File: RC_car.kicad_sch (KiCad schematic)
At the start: 31 parts, among them J1 Conn_02x04_Row_Letter_First, J10 Conn_01x01, J11 MP1584_IN+, J12 MP1584_IN-, J13 MP1584_OUT-, J14 MP1584_OUT+, J2 Screw_Terminal_01x02, J3 Screw_Terminal_01x02, J4 Conn_01x03, J7 Conn_01x01, J8 Conn_01x01, J9 Conn_01x01, U2 L298N, U3 LM2596T-5

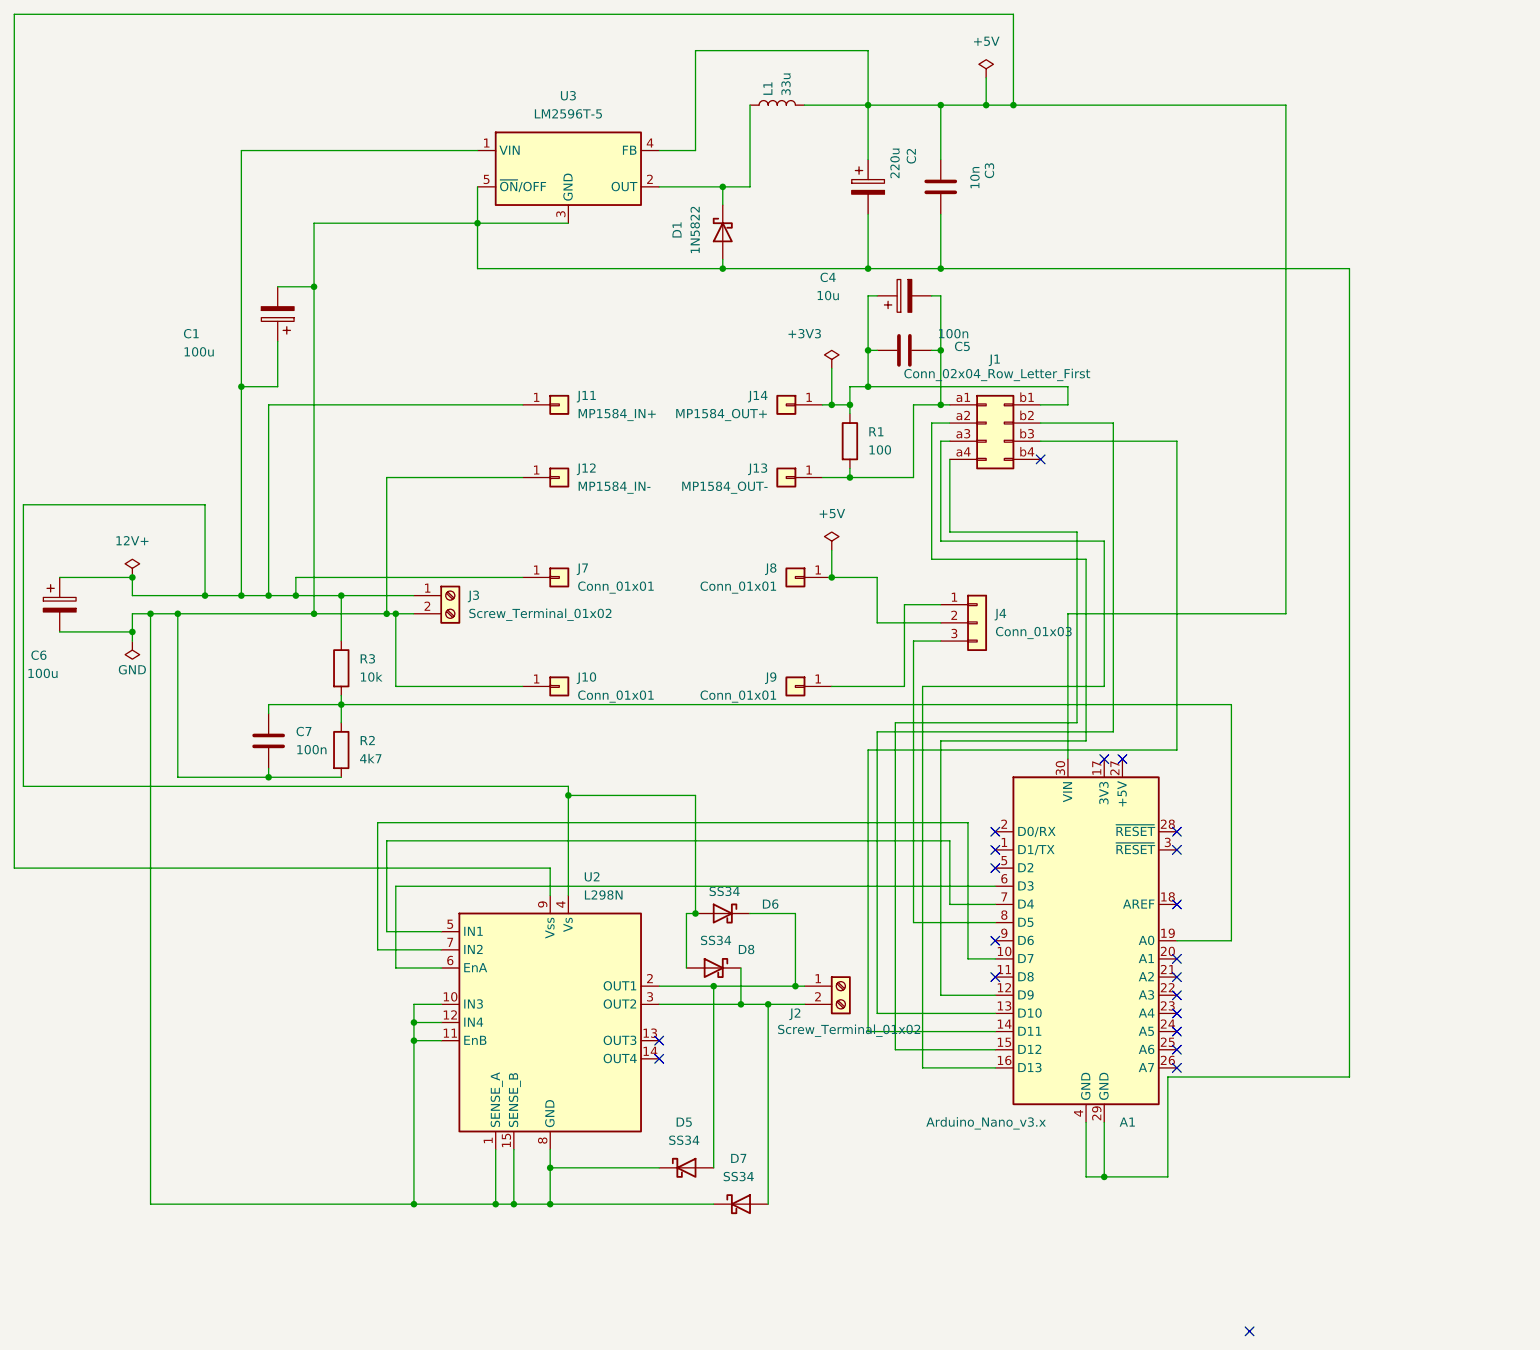
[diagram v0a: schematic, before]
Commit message: Fixed diodes orientation, rework grounding
- reversed all 4 SS34 flyback diodes on L298N outputs
- Nano now powered via 5V pin instead of VIN
- unified ground islands with power:GND symbols
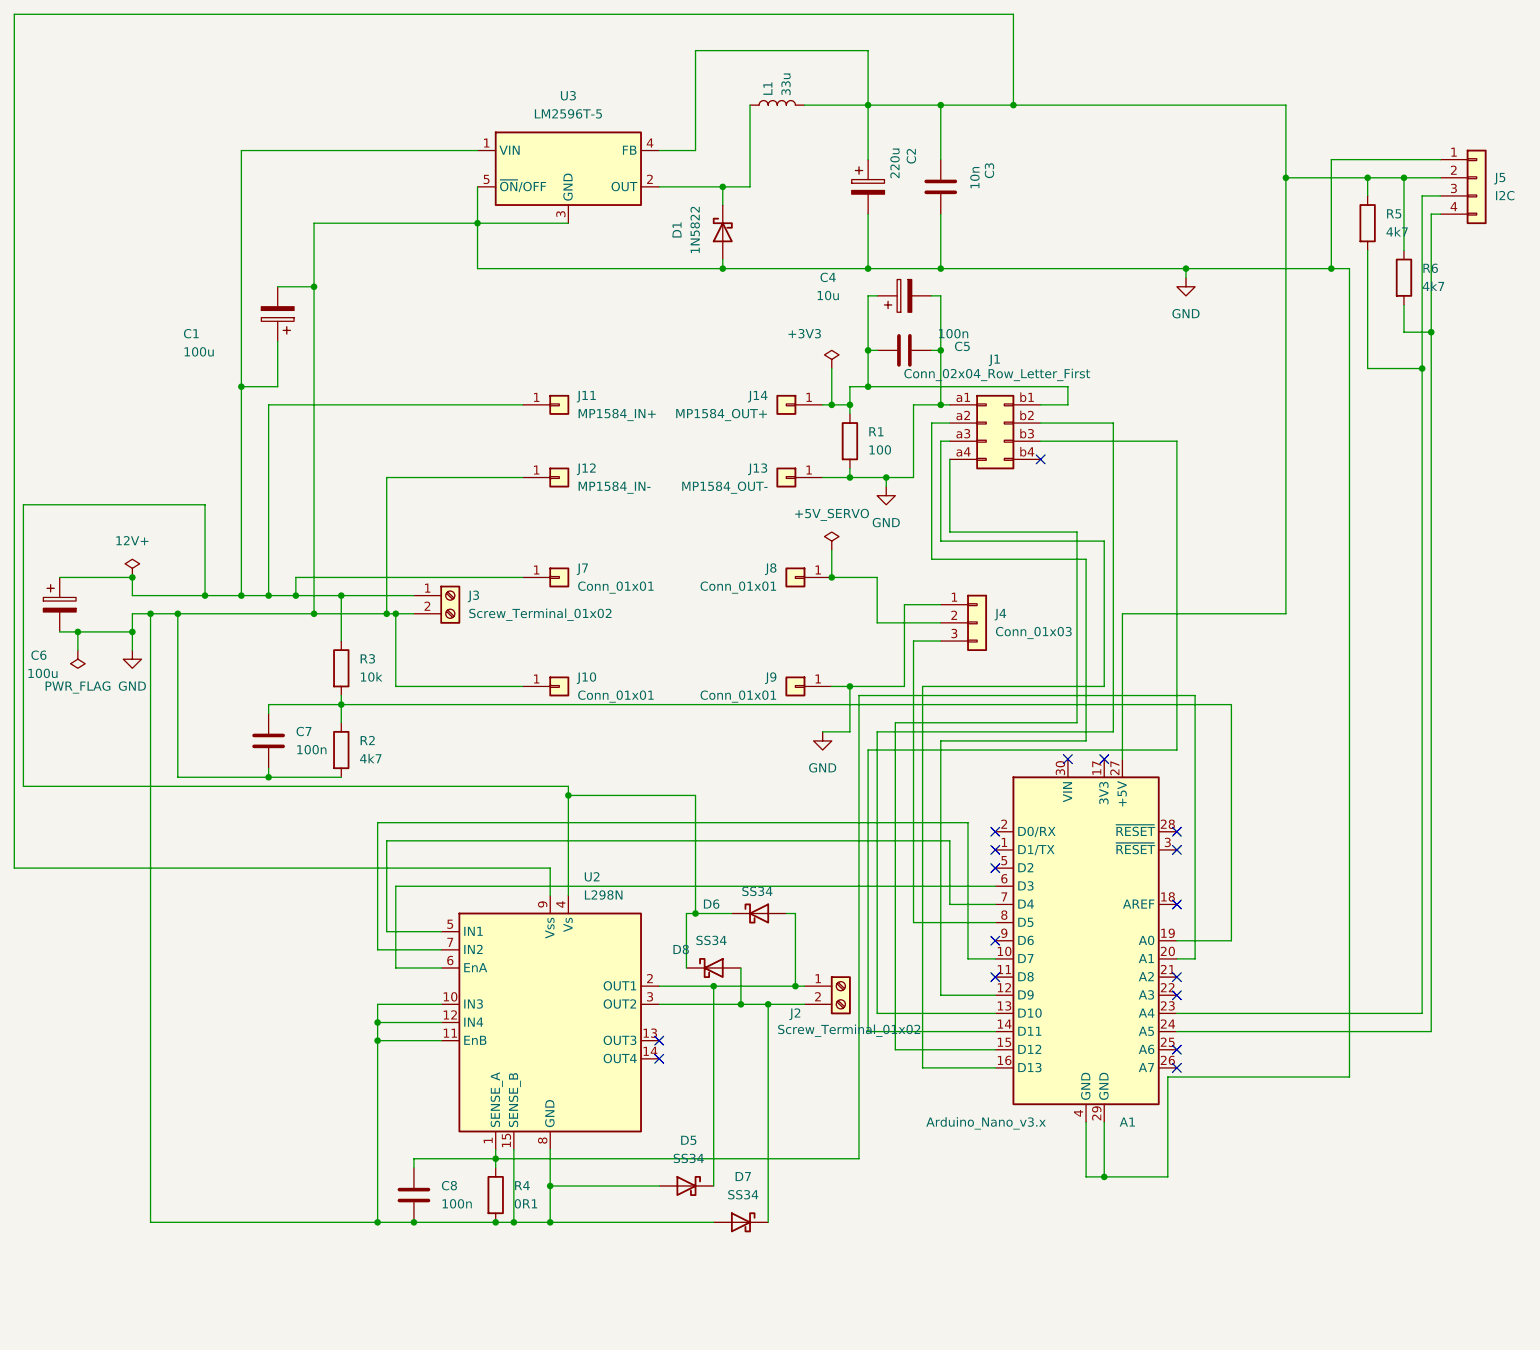
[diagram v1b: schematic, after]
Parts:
- added C8: 100n, symbol Device:C
- added J5: I2C, symbol Connector_Generic:Conn_01x04
- added R4: 0R1, symbol Device:R
- added R5, R6: 4k7, symbol Device:R
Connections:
- net at C1.1, C6.1, J11.1 (Pin_1)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: now also D6.1 (K), D8.1 (K); no longer D6.2 (A), D8.2 (A)
- net GND: now reaches A1.29 (GND), A1.4 (GND), C1.2, C2.2, C3.2, C6.2, C7.2, D1.2 (A), J10.1 (Pin_1), J12.1 (Pin_1), J3.2 (Pin_2), R2.2, U2.10 (IN3), U2.11 (EnB), U2.12 (IN4), U2.15 (SENSE_B), U2.8 (GND), U3.3 (GND), U3.5 (~{ON}/OFF)
- net GND: now also C4.2, C5.1, D5.2 (A), D7.2 (A), J1.a1 (Pin_a1), J13.1 (Pin_1), J4.1 (Pin_1), J9.1 (Pin_1), R1.2, C8.2, J5.1 (Pin_1), R4.2; no longer D5.1 (K), D7.1 (K), U2.1 (SENSE_A)
- net at J2.1 (Pin_1), U2.2 (OUT1): now also D5.1 (K), D6.2 (A); no longer D5.2 (A), D6.1 (K)
- net at C2.1, C3.1, L1.2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: now also A1.27 (+5V), J5.2 (Pin_2), R5.1, R6.1; no longer A1.30 (VIN)
- net at J2.2 (Pin_2), U2.3 (OUT2): now also D7.1 (K), D8.2 (A); no longer D7.2 (A), D8.1 (K)
- net at A1.20 (A1): now also U2.1 (SENSE_A), C8.1, R4.1
- net at A1.23 (A4): now also J5.3 (Pin_3), R5.2
- net at A1.24 (A5): now also J5.4 (Pin_4), R6.2
- no-connect marks 21 -> 17
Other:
- moved on the sheet: D5, D6, D7

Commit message: Improve schematic readability
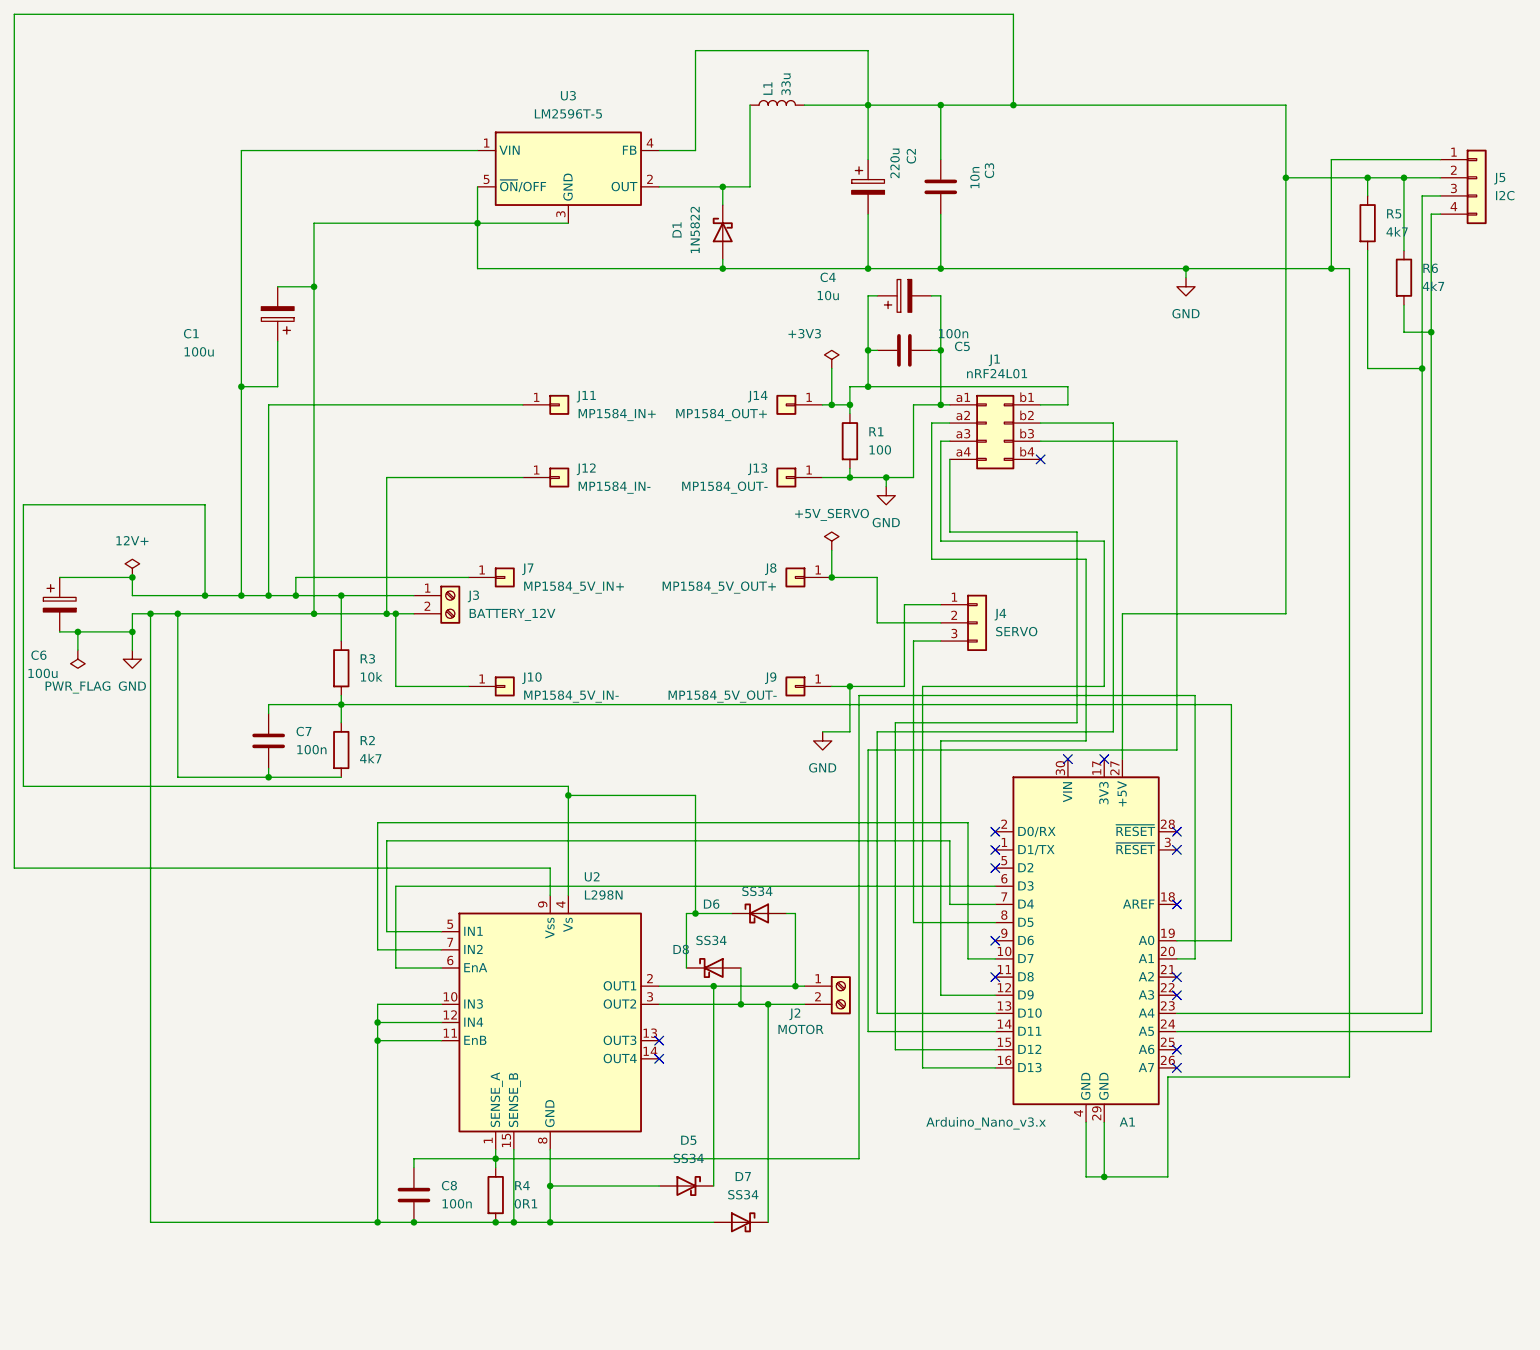
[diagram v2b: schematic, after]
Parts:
- J1: value Conn_02x04_Row_Letter_First -> nRF24L01
- J10: value Conn_01x01 -> MP1584_5V_IN-
- J2: value Screw_Terminal_01x02 -> MOTOR
- J3: value Screw_Terminal_01x02 -> BATTERY_12V
- J4: value Conn_01x03 -> SERVO
- J7: value Conn_01x01 -> MP1584_5V_IN+
- J8: value Conn_01x01 -> MP1584_5V_OUT+
- J9: value Conn_01x01 -> MP1584_5V_OUT-
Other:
- moved on the sheet: J10, J7
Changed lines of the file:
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@@
 	(wire
 		(pts
-			(xy 85.09 95.25) (xy 53.34 95.25)
+			(xy 77.47 95.25) (xy 53.34 95.25)
 		)
 		(stroke
@@
 	(wire
 		(pts
-			(xy 85.09 110.49) (xy 67.31 110.49)
+			(xy 77.47 110.49) (xy 67.31 110.49)
 		)
 		(stroke
@@
 			)
 		)
-		(property "Value" "Screw_Terminal_01x02"
+		(property "Value" "BATTERY_12V"
 			(at 77.47 100.3299 0)
 			(show_name no)
@@
 	(symbol
 		(lib_id "Connector_Generic:Conn_01x01")
-		(at 90.17 110.49 0)
+		(at 82.55 110.49 0)
 		(unit 1)
 		(body_style 1)
@@
 		(fields_autoplaced yes)
 		(property "Reference" "J10"
-			(at 92.71 109.2199 0)
+			(at 85.09 109.2199 0)
 			(show_name no)
 			(do_not_autoplace no)
@@
 			)
 		)
-		(property "Value" "Conn_01x01"
-			(at 92.71 111.7599 0)
+		(property "Value" "MP1584_5V_IN-"
+			(at 85.09 111.7599 0)
 			(show_name no)
 			(do_not_autoplace no)
@@
 		)
 		(property "Footprint" ""
-			(at 90.17 110.49 0)
+			(at 82.55 110.49 0)
 			(hide yes)
 			(show_name no)
@@
 		)
 		(property "Datasheet" ""
-			(at 90.17 110.49 0)
+			(at 82.55 110.49 0)
 			(hide yes)
 			(show_name no)
@@
 		)
 		(property "Description" "Generic connector, single row, 01x01, script generated (kicad-library-utils/schlib/autogen/connector/)"
-			(at 90.17 110.49 0)
+			(at 82.55 110.49 0)
 			(hide yes)
 			(show_name no)
@@
 			)
 		)
-		(property "Value" "Screw_Terminal_01x02"
+		(property "Value" "MOTOR"
 			(at 120.65 158.496 0)
 			(show_name no)
@@
 	(symbol
 		(lib_id "Connector_Generic:Conn_01x01")
-		(at 90.17 95.25 0)
+		(at 82.55 95.25 0)
 		(unit 1)
 		(body_style 1)
@@
 		(fields_autoplaced yes)
 		(property "Reference" "J7"
-			(at 92.71 93.9799 0)
+			(at 85.09 93.9799 0)
 			(show_name no)
 			(do_not_autoplace no)
@@
 			)
 		)
-		(property "Value" "Conn_01x01"
-			(at 92.71 96.5199 0)
+		(property "Value" "MP1584_5V_IN+"
+			(at 85.09 96.5199 0)
 			(show_name no)
 			(do_not_autoplace no)
@@
 		)
 		(property "Footprint" ""
-			(at 90.17 95.25 0)
+			(at 82.55 95.25 0)
 			(hide yes)
 			(show_name no)
@@
 		)
 		(property "Datasheet" ""
-			(at 90.17 95.25 0)
+			(at 82.55 95.25 0)
 			(hide yes)
 			(show_name no)
@@
 		)
 		(property "Description" "Generic connector, single row, 01x01, script generated (kicad-library-utils/schlib/autogen/connector/)"
-			(at 90.17 95.25 0)
+			(at 82.55 95.25 0)
 			(hide yes)
 			(show_name no)
@@
 			)
 		)
-		(property "Value" "Conn_01x01"
+		(property "Value" "MP1584_5V_OUT-"
 			(at 120.65 111.7599 0)
 			(show_name no)
@@
 			)
 		)
-		(property "Value" "Conn_01x01"
+		(property "Value" "MP1584_5V_OUT+"
 			(at 120.65 96.5199 0)
 			(show_name no)
@@
 			)
 		)
-		(property "Value" "Conn_02x04_Row_Letter_First"
+		(property "Value" "nRF24L01"
 			(at 151.384 66.802 0)
 			(show_name no)
@@
 			)
 		)
-		(property "Value" "Conn_01x03"
+		(property "Value" "SERVO"
 			(at 151.13 102.8699 0)
 			(show_name no)
